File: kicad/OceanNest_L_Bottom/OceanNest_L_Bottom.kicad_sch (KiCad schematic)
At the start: 34 parts, among them J1 TRRS_MJ-4PP-9, SW1 SW_Push, SW10 SW_Push, SW11 SW_Push, SW12 SW_Push, SW13 SW_Push, SW14 RotaryEncoder, SW2 SW_Push, SW3 SW_Push, SW4 SW_Push, SW5 SW_Push, SW6 SW_Push, SW7 SW_Push, SW8 SW_Push, SW9 SW_Push, U1 XIAO-RP2040-DIP

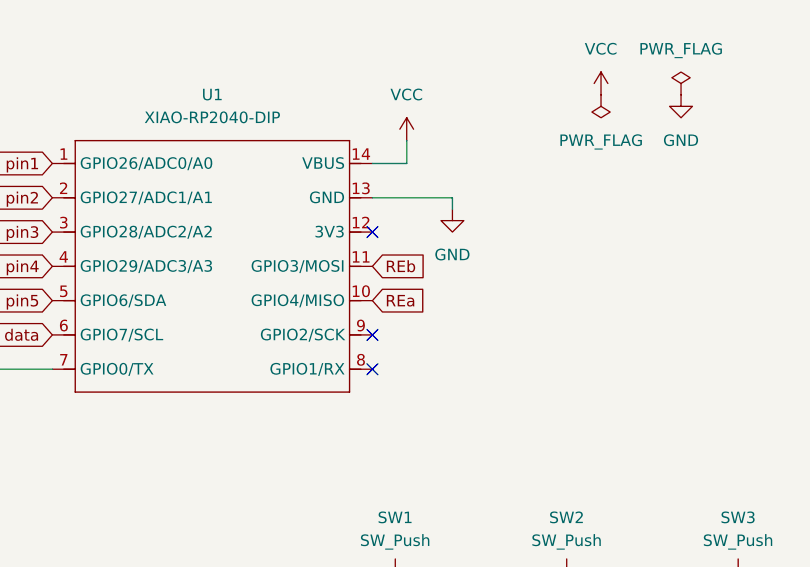
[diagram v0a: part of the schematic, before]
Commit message: feat: add new PCB and schematic files for OceanNest_L and OceanNest_L_Bottom, including layout adjustments and component updates
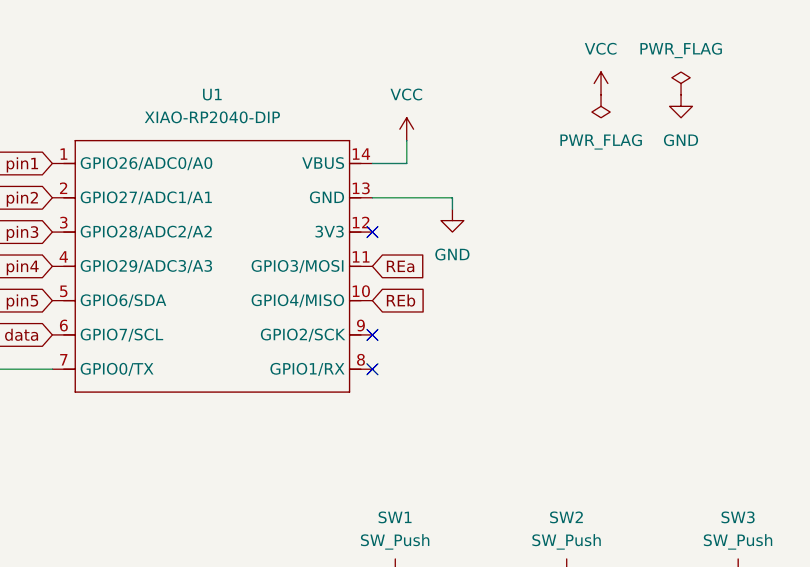
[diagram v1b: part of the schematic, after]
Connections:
- net REa: now also U1.11 (GPIO3/MOSI); no longer U1.10 (GPIO4/MISO)
- net REb: now also U1.10 (GPIO4/MISO); no longer U1.11 (GPIO3/MOSI)
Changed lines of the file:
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@@
 	(global_label "REa"
 		(shape input)
-		(at 82.55 49.53 0)
+		(at 82.55 45.72 0)
 		(fields_autoplaced yes)
 		(effects
@@
 		)
 		(property "Intersheetrefs" "${INTERSHEET_REFS}"
-			(at 89.1032 49.53 0)
+			(at 89.1032 45.72 0)
 			(effects
 				(font
@@
 	(global_label "REb"
 		(shape input)
-		(at 82.55 45.72 0)
+		(at 82.55 49.53 0)
 		(fields_autoplaced yes)
 		(effects
@@
 		)
 		(property "Intersheetrefs" "${INTERSHEET_REFS}"
-			(at 89.1032 45.72 0)
+			(at 89.1032 49.53 0)
 			(effects
 				(font
